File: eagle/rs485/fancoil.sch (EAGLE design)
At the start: 23 parts, among them J1 1-770166-0, J13 FEMALE 2x3, J4 JST-XH-04-PIN-ROUND-PAD, Q1 600mA/40V, U1 AP63203WU-7, U2 LTV-814S, U3 ATTINY426-MU, U9 SP3485CN-L

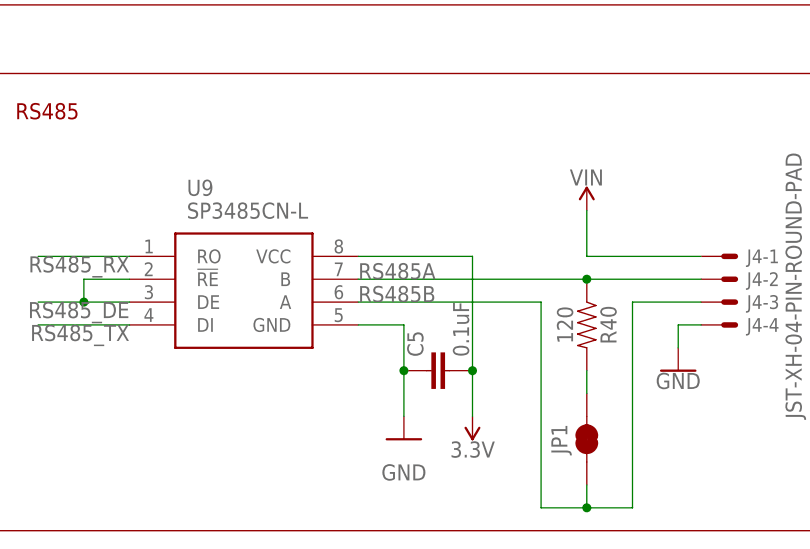
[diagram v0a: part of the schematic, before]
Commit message: finish flipping RS485A/B
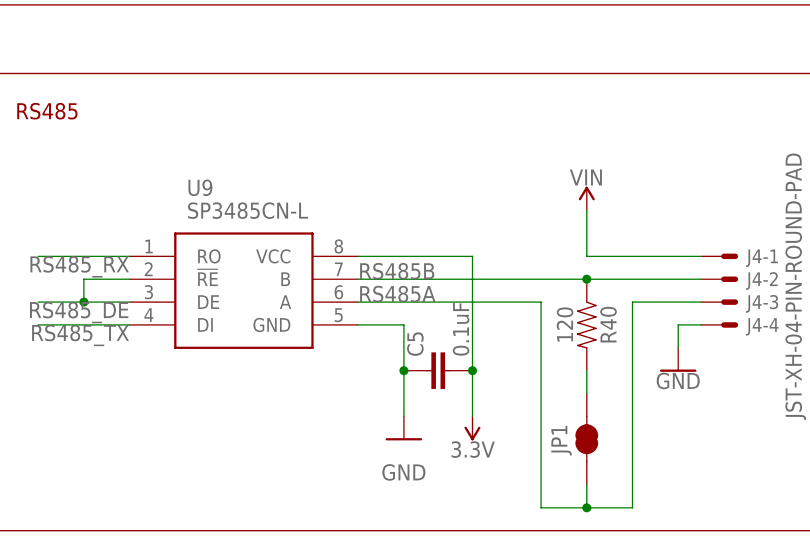
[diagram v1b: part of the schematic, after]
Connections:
- net RS485A: now also J4-3.S, JP1.1, U9.A; no longer J4-2.S, R40.1, U9.B
- net RS485B: now also J4-2.S, R40.1, U9.B; no longer J4-3.S, JP1.1, U9.A
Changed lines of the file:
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@@
 </segment>
 </net>
-<net name="RS485B" class="0">
+<net name="RS485A" class="0">
 <segment>
 <label x="83.82" y="5.08" size="1.778" layer="95"/>
@@
 </segment>
 </net>
-<net name="RS485A" class="0">
+<net name="RS485B" class="0">
 <segment>
 <wire x1="83.82" y1="7.62" x2="109.22" y2="7.62" width="0.1524" layer="91"/>
